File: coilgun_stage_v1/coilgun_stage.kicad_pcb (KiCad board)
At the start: 2 copper layers, 36 x 36 mm, 16 parts, among them J1 Conn_01x05_Female, J2 Conn_01x05_Female, Q1 MMBT5551L, Q2 LTR-4206E

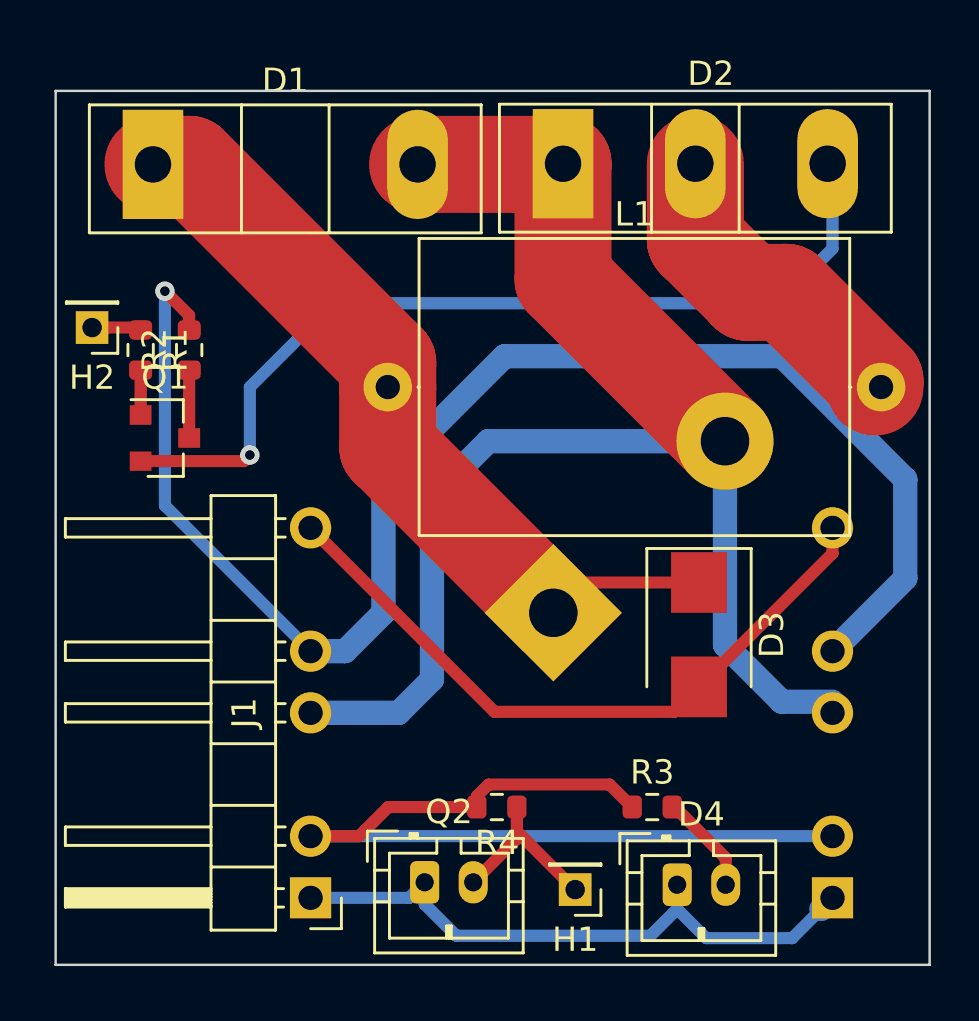
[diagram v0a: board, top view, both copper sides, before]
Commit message: Increase track clearance, cosmetic fixes
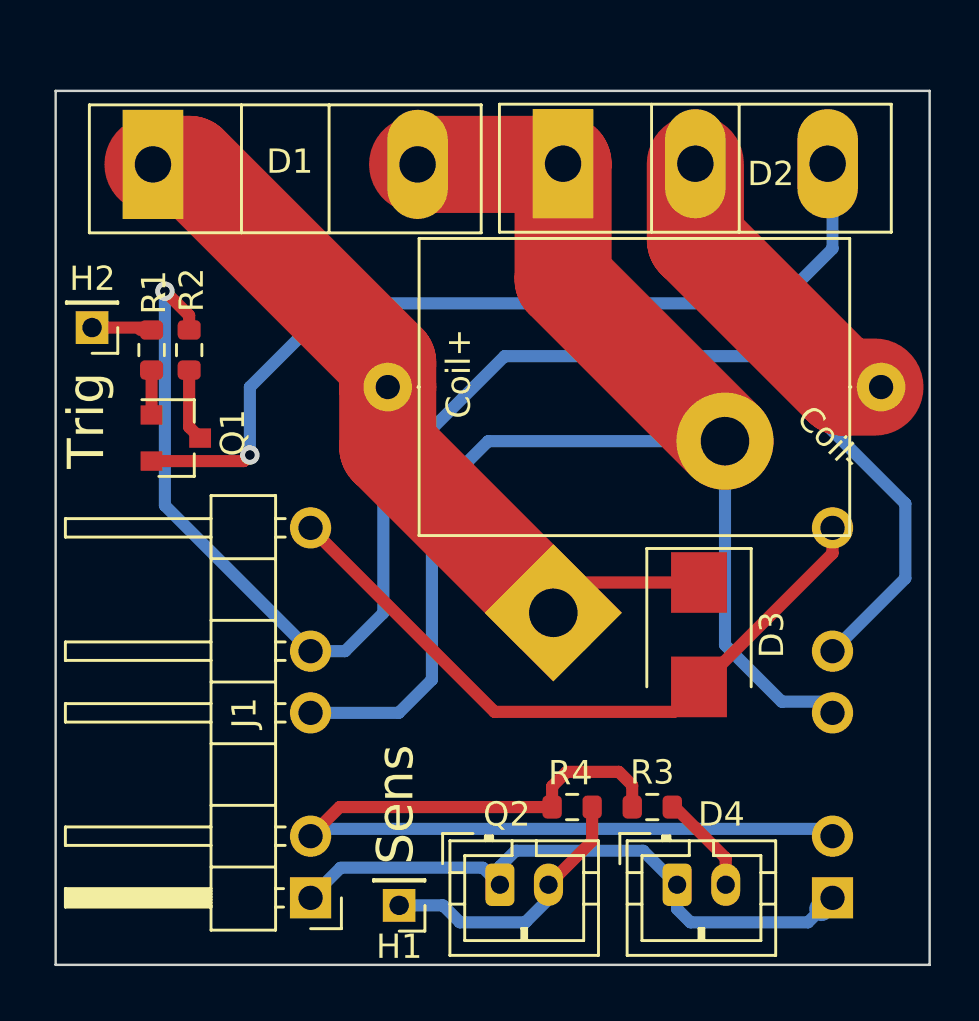
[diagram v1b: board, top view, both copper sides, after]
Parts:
- moved H1 7.28 mm to (61.1, 72.5)
- moved Q2 3.10 mm to (65.3, 71.7)
- moved R4 3.10 mm to (68.3, 68.5)
- moved Q1 0.45 mm to (52.0, 53.3)
- moved R1 0.45 mm to (51.0, 49.7)
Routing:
- net SENS: track 8.24 -> 11.4 mm
- net +3V3: track 36.7 -> 38.1 mm
- net TRIG: track 2.04 -> 2.94 mm
- net +3.3VP: track 62.6 -> 62.0 mm
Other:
- board text added: "Coil+"
- board text added: "Coil-"
- board text added: "Sens"
- board text added: "Trig"

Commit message: Get rid of the useless optocoupler
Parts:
- R1, R2, R3, R4: footprint Resistor_SMD:R_0603_1608Metric -> Resistor_SMD:R_0603_1608Metric_Pad0.98x0.95mm_HandSolder

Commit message: Fix swapped labels
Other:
- board text added: "3V3"
- board text added: "3V3P"
- board text added: "400V"
- board text added: "GND"
- board text added: "GNDP"
